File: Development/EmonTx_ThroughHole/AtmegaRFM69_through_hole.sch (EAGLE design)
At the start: 50 parts, among them CN1 AC 9V, IC1 ATMEGA 328, IC2 MCP1702, J1 1X2-3.5MM, J2 1X2-3.5MM, J3 1X2-3.5MM

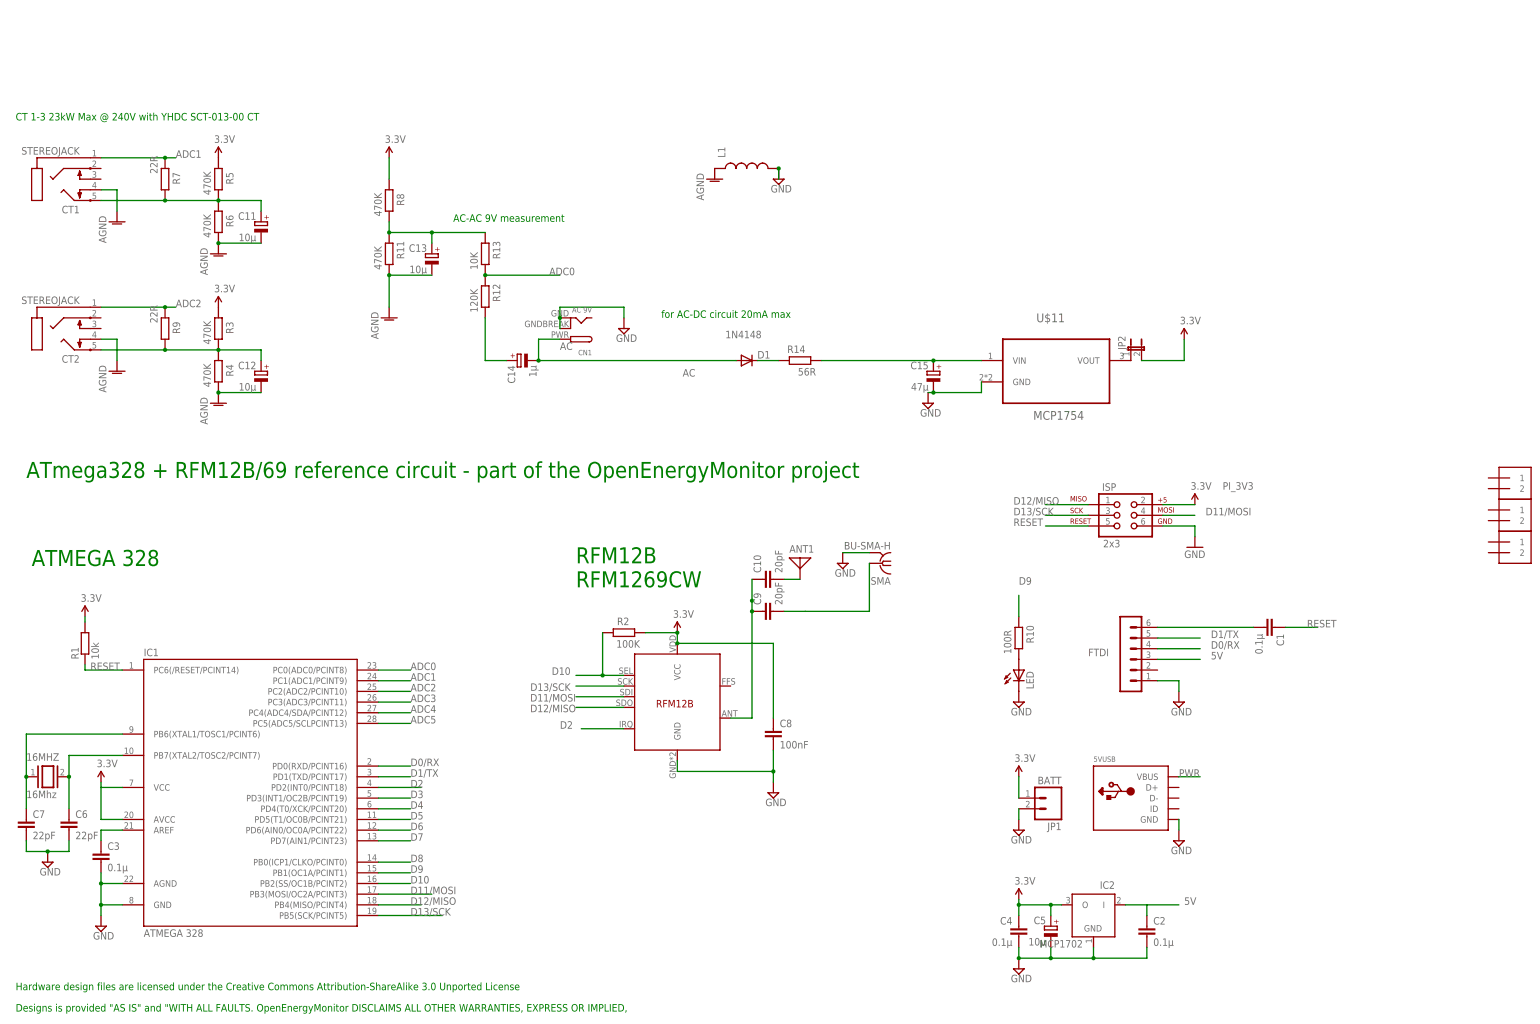
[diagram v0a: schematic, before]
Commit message: Single voltage regulator, power supply test results, usb positioning
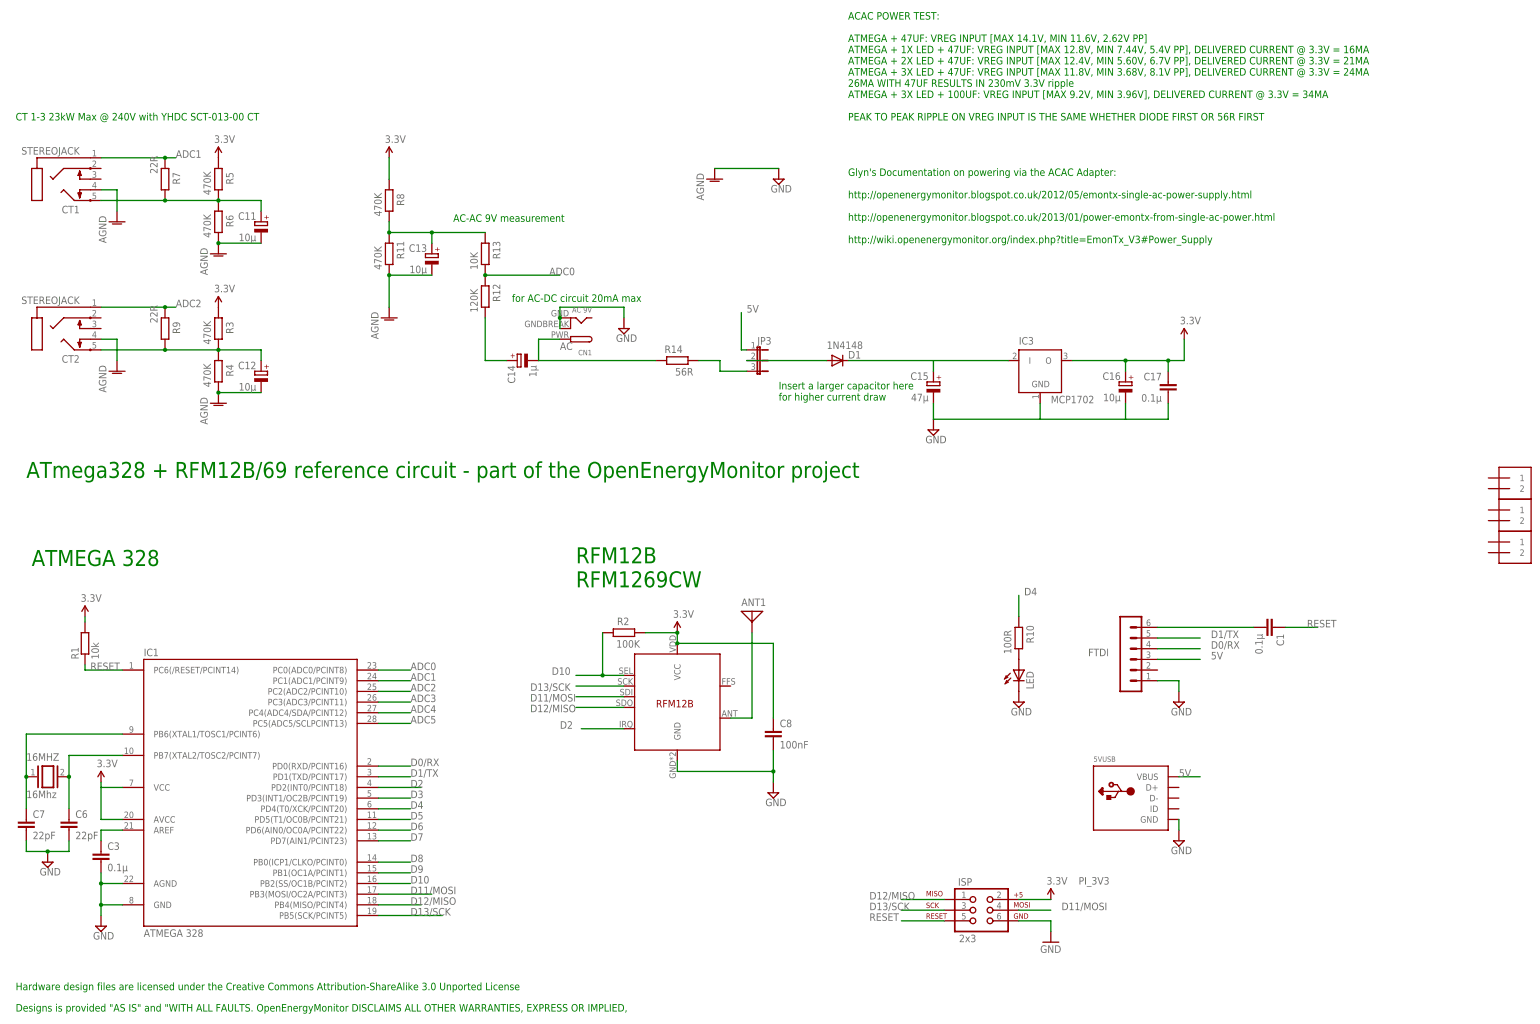
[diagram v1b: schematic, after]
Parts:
- removed C10, C9: 20pF, resistor:C-EU025-024X044
- removed C2, C4: 0.1µ, resistor:C-EU025-024X044
- removed C5: 10µ, resistor:CPOL-EUE1.8-4
- removed IC2: MCP1702, JeeLabs:MCP1702Z
- removed JP1: BATT, SparkFun:M02LOCK_LONGPADS
- removed JP2: (no value), SparkFun:JUMPER-2PTH_LOCK
- removed L1: (no value), SparkFun:INDUCTOR0603
- removed SMA: BU-SMA-H, con-coax:BU-SMA-H
- removed U$11: MCP1754, OpenEnergyMonitor:MCP1754
- added C16: 10µ, resistor:CPOL-EUE1.8-4
- added C17: 0.1µ, resistor:C-EU025-024X044
- added IC3: MCP1702, JeeLabs:MCP1702Z
- added JP3: (no value), jumper:JP2E
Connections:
- removed net N$11: ANT1.1, C10.2
- removed net N$24: C9.2, SMA.1
- removed net N$6: C15.+, R14.1, U$11.VIN
- removed net PWR: 5VUSB.VBUS
- new net N$4: C15.+, D1.C, IC3.I
- net 3.3V: now also C16.+, C17.1, IC3.O; no longer C4.1, C5.+, IC2.O, JP1.1, JP2.2
- net 5V: now also 5VUSB.VBUS, JP3.1; no longer C2.1, IC2.I
- net AC: now also R14.2; no longer D1.A
- net AGND: no longer L1.1
- net D4: now also R10.2
- net D9: no longer R10.2
- net DIG1: now also ANT1.1; no longer C10.1, C9.1
- net GND: now also C16.-, C17.2, IC3.GND; no longer C2.2, C4.2, C5.-, IC2.GND, JP1.2, L1.2, SMA.2, U$11.GND
- net N$3: now also JP3.3, R14.1; no longer D1.C, R14.2
- net N$5: now also D1.A, JP3.2; no longer JP2.1, U$11.VOUT
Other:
- note added: "ACAC POWER TEST: ATMEGA + 47UF: VREG INPUT [MAX 14.1V, MIN 11.6V, 2.62V PP] ATMEGA + 1X LED + 47UF: VREG INPUT [MAX 12.8V, MIN 7.44V, 5.4V PP], DELIVERED CURRENT @ 3.3V = 16MA ATMEGA + 2X LED + 47UF: VREG INPUT [MAX 12.4V, MIN 5.60V, 6.7V PP], DELIVERED CURRENT @ 3.3V = 21MA ATMEGA + 3X LED + 47UF: VREG INPUT [MAX 11.8V, MIN 3.68V, 8.1V PP], DELIVERED CURRENT @ 3.3V = 24MA 26MA WITH 47UF RESULTS 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"
- note added: "Glyn's Documentation on powering via the ACAC Adapter: http://openenergymonitor.blogspot.co.uk/2012/05/emontx-single-ac-power-supply.html http://openenergymonitor.blogspot.co.uk/2013/01/power-emontx-from-single-ac-power.html http://wiki.openenergymonitor.org/index.php?title=EmonTx_V3#Power_Supply"
- note added: "Insert a larger capacitor here for higher current draw"
- moved on the sheet: ANT1, C15, D1, ISP, R14
